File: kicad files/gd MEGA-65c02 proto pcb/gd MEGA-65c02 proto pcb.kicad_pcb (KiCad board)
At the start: 2 copper layers, 54 parts, among them J1 Pwr, J2 CTRL2, J3 Addr_Main_Data, J4 CTRL1, J5 Slot_Maker, J6 Aux Data_La, J7 CLKS, J8 14M_SEL, J9 PWR, Q1 Q_NPN_BCE-GET PACKAGE!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

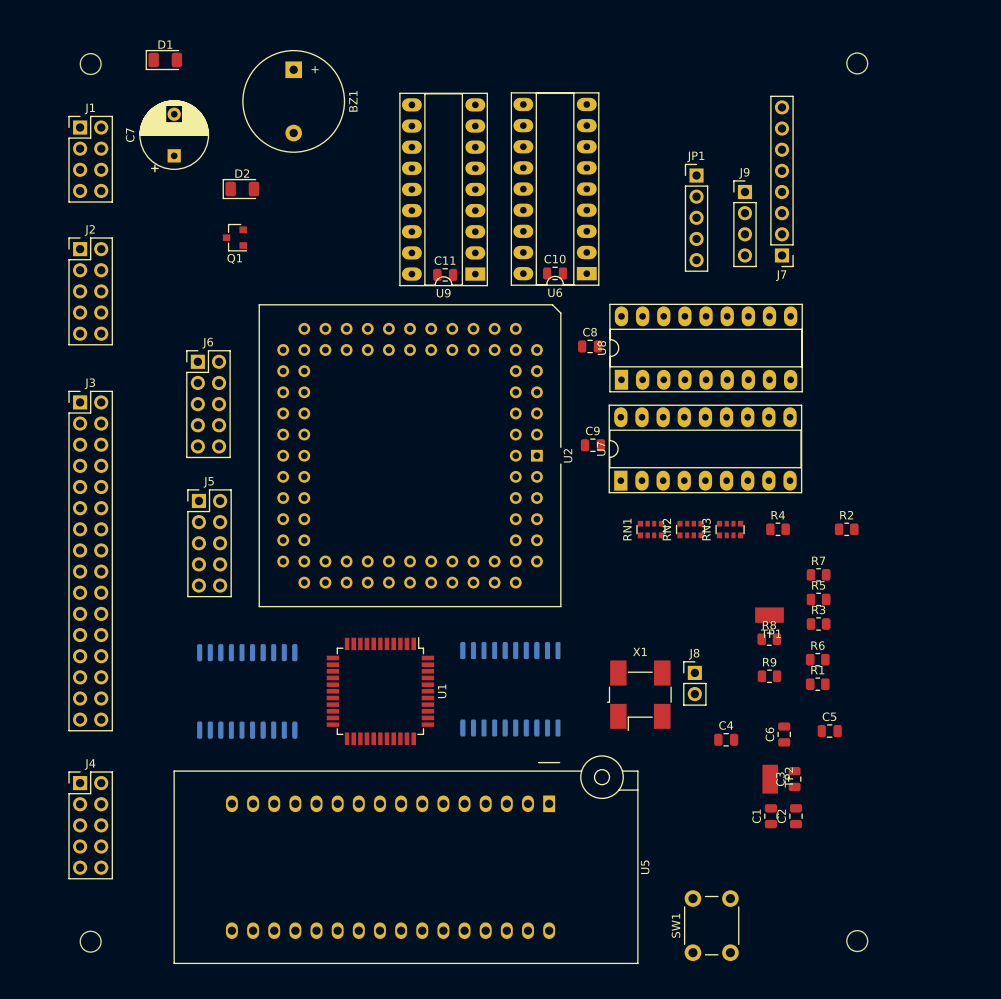
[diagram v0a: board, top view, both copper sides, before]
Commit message: started rev2 mega-6502 board design
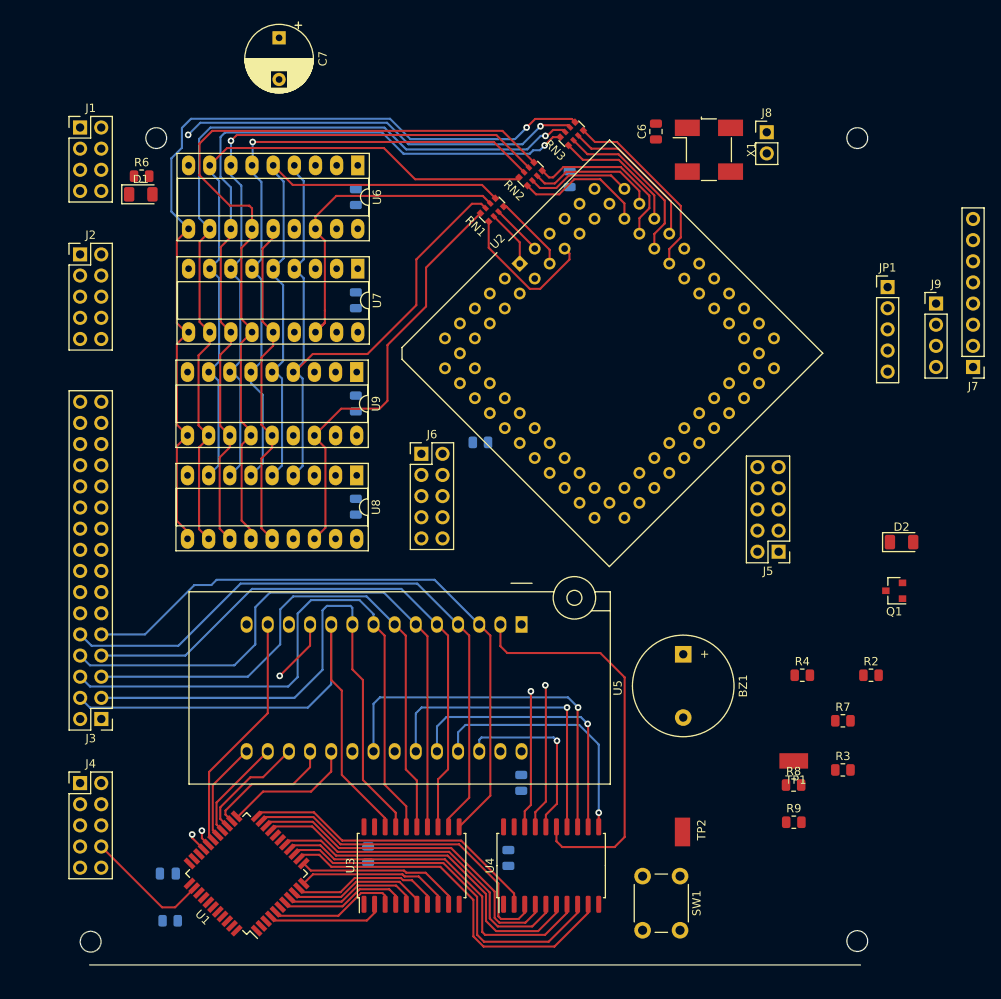
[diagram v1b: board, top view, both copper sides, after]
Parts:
- C1, C10, C11, C2, C3, C4, C5, C8, C9, R1, R5: moved to B.Cu
- U3, U4: moved to F.Cu
- U5: footprint Socket:DIP_Socket-32_W11.9_W12.7_W15.24_W17.78_W18.5_3M_232-1285-00-0602J -> Socket:DIP_Socket-28_W11.9_W12.7_W15.24_W17.78_W18.5_3M_228-1277-00-0602J
- moved R6 99.8 mm to (50.6, 52.2)
- moved D2 89.8 mm to (141.8, 96.2)
- moved Q1 89.8 mm to (141.0, 102.0)
- moved BZ1 84.4 mm to (115.6, 109.6)
- moved R1 82.8 mm to (54.0, 141.6)
- moved C6 74.0 mm to (112.3, 46.8)
- moved C5 73.3 mm to (102.0, 52.6), turned to 90 degrees
- moved J5 69.9 mm to (127.1, 97.3), turned to 180 degrees
- moved C4 69.0 mm to (53.7, 136.0), turned to 180 degrees
- moved X1 66.0 mm to (118.7, 49.0), turned to 270 degrees
- moved J8 65.5 mm to (125.7, 46.9)
- moved C2 51.6 mm to (77.8, 133.7), turned to 270 degrees
- moved RN3 51.2 mm to (102.2, 47.1), turned to 135 degrees
- moved RN2 46.8 mm to (97.3, 51.9), turned to 135 degrees
- moved R5 44.8 mm to (91.3, 84.2)
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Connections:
- RN1 pad 1: /CASM -> /CASA
- RN1 pad 2: /CASA -> /RAMWE
- RN1 pad 3: /RAS -> /CASM
- RN1 pad 4: /RAMWE -> /RAS
- RN1 pad 5: /RWE.B -> /RAS.B
- RN1 pad 6: /RAS.B -> /CASM.B
- RN1 pad 7: /CASA.B -> /RWE.B
- RN1 pad 8: /CASM.B -> /CASA.B
- RN2 pad 1: /RA0 -> /RA1
- RN2 pad 2: /RA3 -> /RA0
- RN2 pad 3: /RA6 -> /RA2
- RN2 pad 4: /RA7 -> /RA3
- RN2 pad 5: /RAF7 -> /RAF3
- RN2 pad 6: /RAF6 -> /RAF2
- RN2 pad 7: /RAF3 -> /RAF0
- RN2 pad 8: /RAF0 -> /RAF1
- RN3 pad 1: /RA1 -> /RA4
- RN3 pad 3: /RA2 -> /RA6
- RN3 pad 4: /RA4 -> /RA7
- RN3 pad 5: /RAF4 -> /RAF7
- RN3 pad 6: /RAF2 -> /RAF6
- RN3 pad 8: /RAF1 -> /RAF4
- U3 pad 11: /BA0 -> /BA7
- U3 pad 12: /BA1 -> /BA6
- U3 pad 13: /BA2 -> /BA5
- U3 pad 14: /BA3 -> /BA4
- U3 pad 15: /BA4 -> /BA3
- U3 pad 16: /BA5 -> /BA2
- U3 pad 17: /BA6 -> /BA1
- U3 pad 18: /BA7 -> /BA0
- U3 pad 2: /A7 -> /A0
- U3 pad 3: /A6 -> /A1
- U3 pad 4: /A5 -> /A2
- U3 pad 5: /A4 -> /A3
- U3 pad 6: /A3 -> /A4
- U3 pad 7: /A2 -> /A5
- U3 pad 8: /A1 -> /A6
- U3 pad 9: /A0 -> /A7
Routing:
- net /MD5: track 0.00 -> 187.7 mm
- net /MD1: track 0.00 -> 185.1 mm, vias 0 -> 1
- net /MD0: track 0.00 -> 179.6 mm, vias 0 -> 2
- net /MD7: track 0.00 -> 178.5 mm
- net /MD6: track 0.00 -> 168.8 mm
- net /MD2: track 0.00 -> 168.7 mm
- net /MD4: track 0.00 -> 168.5 mm
- net /MD3: track 0.00 -> 146.2 mm
- net /RAF6: track 0.00 -> 109.8 mm, vias 0 -> 2
- net /BA10: track 0.00 -> 107.2 mm, vias 0 -> 1
- net /BA12: track 0.00 -> 104.7 mm
- net /RAF7: track 0.00 -> 104.1 mm, vias 0 -> 1
- net /RAF5: track 0.00 -> 98.3 mm, vias 0 -> 1
- net /BA11: track 0.00 -> 98.3 mm, vias 0 -> 1
- net /RAF3: track 0.00 -> 96.9 mm
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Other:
- copper layers 2 -> 4

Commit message: added address bus to mega-2, routed clocks (minus vgc header), re-routed main data between ROM and backplane connectors, added several missing signals
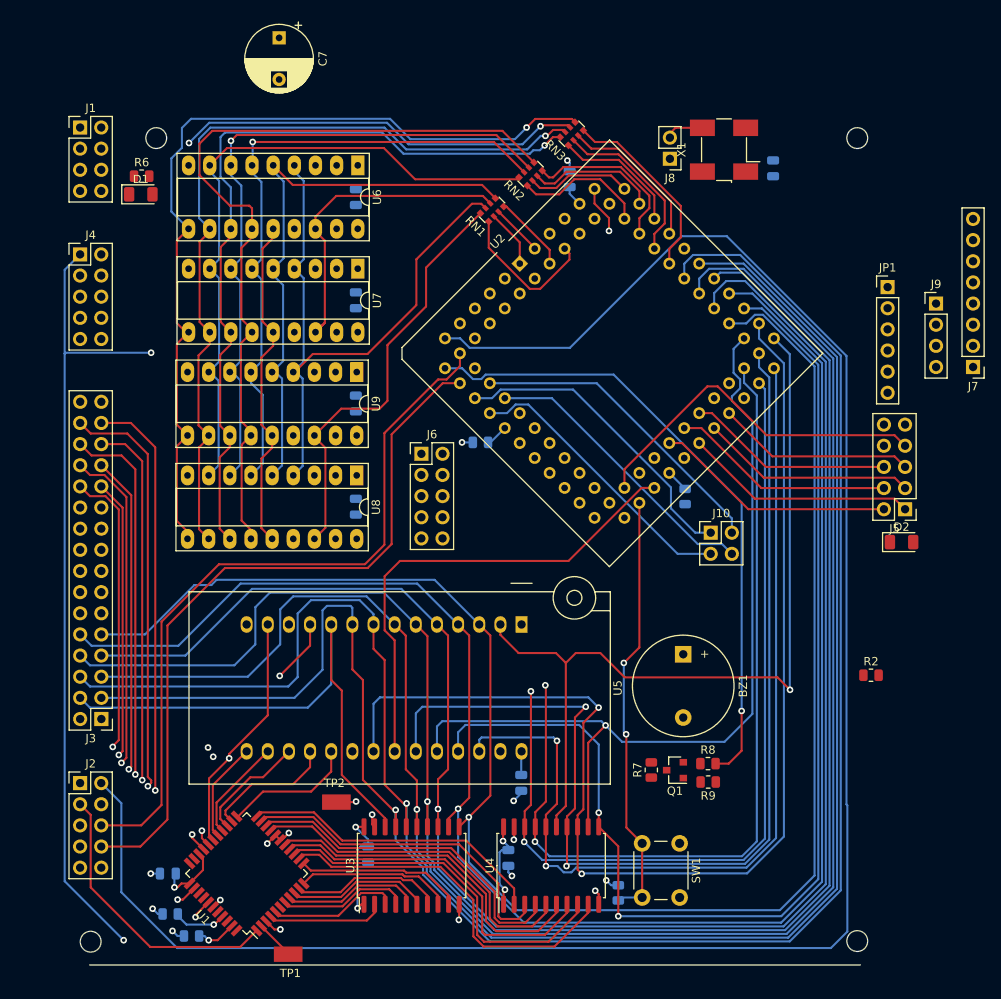
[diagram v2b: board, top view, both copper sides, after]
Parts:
- added J10: XY, Connector_PinHeader_2.54mm:PinHeader_2x02_P2.54mm_Vertical, F.Cu at (118.9, 95.0)
- added R10: 4k7, Resistor_SMD:R_0805_2012Metric, B.Cu at (115.8, 90.7)
- C6, R3, R4: moved to B.Cu
- JP1: footprint Connector_PinHeader_2.54mm:PinHeader_1x05_P2.54mm_Vertical -> Connector_PinHeader_2.54mm:PinHeader_1x06_P2.54mm_Vertical
- R5: value 3k3 -> 4k7
- moved R3 82.6 mm to (54.0, 140.8)
- moved TP1 65.0 mm to (68.2, 145.6)
- moved J2 63.5 mm to (43.2, 125.1)
- moved J4 63.5 mm to (43.2, 61.6)
- moved TP2 41.7 mm to (74.0, 127.4), turned to 180 degrees
- moved R4 34.2 mm to (107.8, 138.3), turned to 270 degrees
- moved Q1 34.0 mm to (114.6, 123.5)
- moved R7 23.8 mm to (111.8, 123.5), turned to 90 degrees
- moved J5 16.0 mm to (142.3, 92.2)
- moved C6 14.7 mm to (126.4, 51.3)
- moved J8 12.1 mm to (114.0, 50.1), turned to 180 degrees
- moved R9 11.4 mm to (118.6, 125.0), turned to 180 degrees
- moved R8 10.6 mm to (118.6, 122.8)
- moved SW1 3.94 mm to (115.2, 132.3)
- moved R1 3.15 mm to (56.6, 143.5)
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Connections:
- J2 pad 5: /!DMA -> /~DMA
- U2 pad 15: /IRQ -> /~IRQ
- U2 pad 37: /ROMEN -> /~ROMEN
- U2 pad 50: /SYNC -> /~SYNC
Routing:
- net /C060-67: track 0.00 -> 234.3 mm
- net /BA1: track 67.5 -> 222.9 mm, vias 0 -> 1
- net /~IRQ: track 0.00 -> 151.2 mm, vias 0 -> 3
- net /BA2: track 72.4 -> 221.7 mm, vias 0 -> 1
- net /PH0: track 15.1 -> 163.5 mm, vias 0 -> 1
- net /BA3: track 68.5 -> 216.8 mm, vias 0 -> 1
- net /BA4: track 73.5 -> 216.4 mm, vias 0 -> 1
- net /BA5: track 70.8 -> 212.1 mm, vias 0 -> 1
- net /BA6: track 77.0 -> 208.7 mm, vias 0 -> 1
- net /BA7: track 76.7 -> 202.2 mm, vias 0 -> 1
- net /~RESET: track 0.00 -> 112.8 mm, vias 0 -> 3
- net /BA8: track 92.4 -> 203.4 mm, vias 1 -> 2
- net /BA10: track 107.2 -> 205.5 mm, vias 1 -> 2
- net /BA11: track 98.3 -> 190.9 mm, vias 1 -> 2
- net /BA13: track 93.6 -> 184.5 mm, vias 1 -> 2
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
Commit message: Changed electrolytic to polymer-ta
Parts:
- added J11: 14M Enable, Connector_PinHeader_2.54mm:PinHeader_1x03_P2.54mm_Vertical, F.Cu at (127.1, 46.4)
- C7: footprint Capacitor_THT:CP_Radial_D8.0mm_P5.00mm -> Capacitor_Tantalum_SMD:CP_EIA-3216-18_Kemet-A_Pad1.58x1.35mm_HandSolder
- moved C6 8.23 mm to (118.8, 54.4), turned to 0 degrees
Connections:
- X1 pad 1: +5V -> Net-(J11-Pad2)
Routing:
- net Net-(J11-Pad2): track 0.00 -> 5.94 mm
- net +5V: track 45.9 -> 50.1 mm, vias 10 -> 11

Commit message: before trying to route clocks for video
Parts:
- BZ1: footprint Buzzer_Beeper:Buzzer_12x9.5RM7.6 -> My Libraries:12mm_Piezo_Buzzer
- C7: moved to B.Cu
- moved C7 23.5 mm to (50.5, 52.2), turned to 0 degrees
- moved BZ1 4.01 mm to (115.7, 113.6)
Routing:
- net +5V: track 50.1 -> 60.1 mm

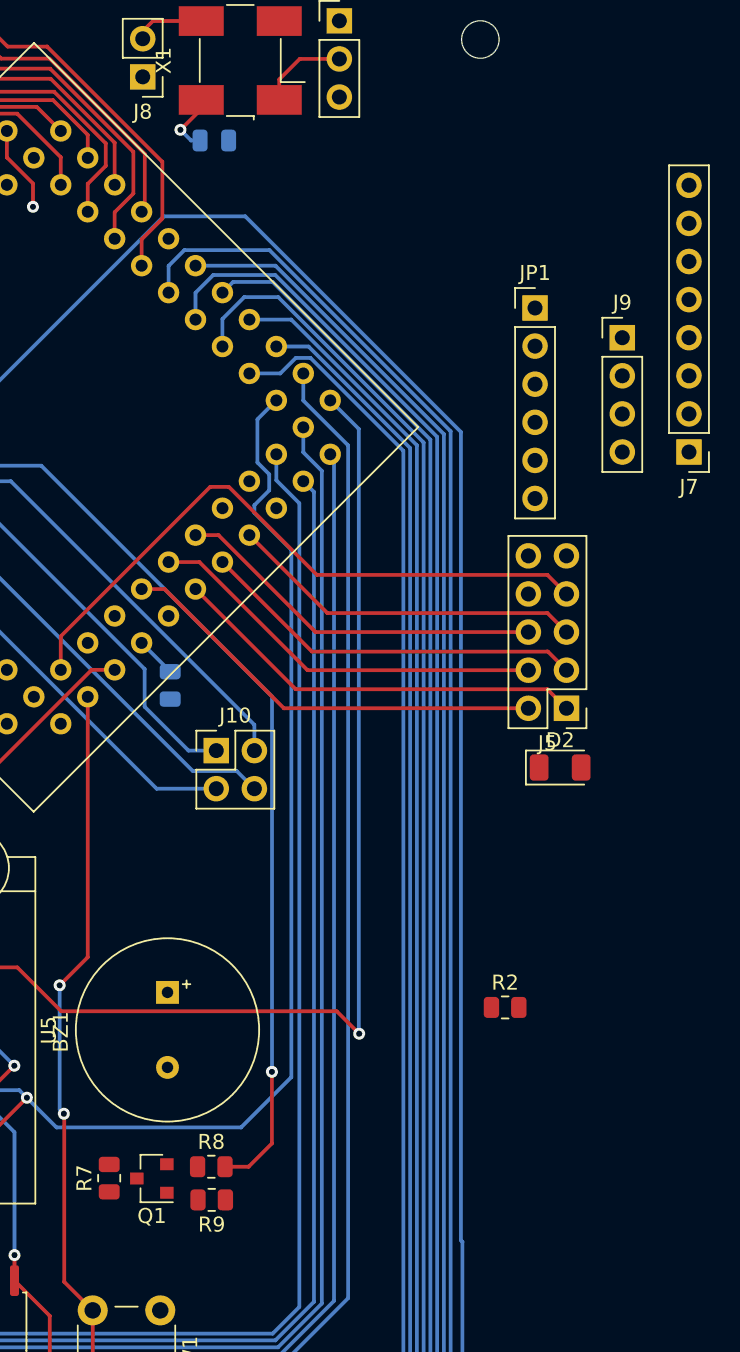
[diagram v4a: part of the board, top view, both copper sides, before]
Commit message: 111 to go: routed video clocks, changed video pin headers.
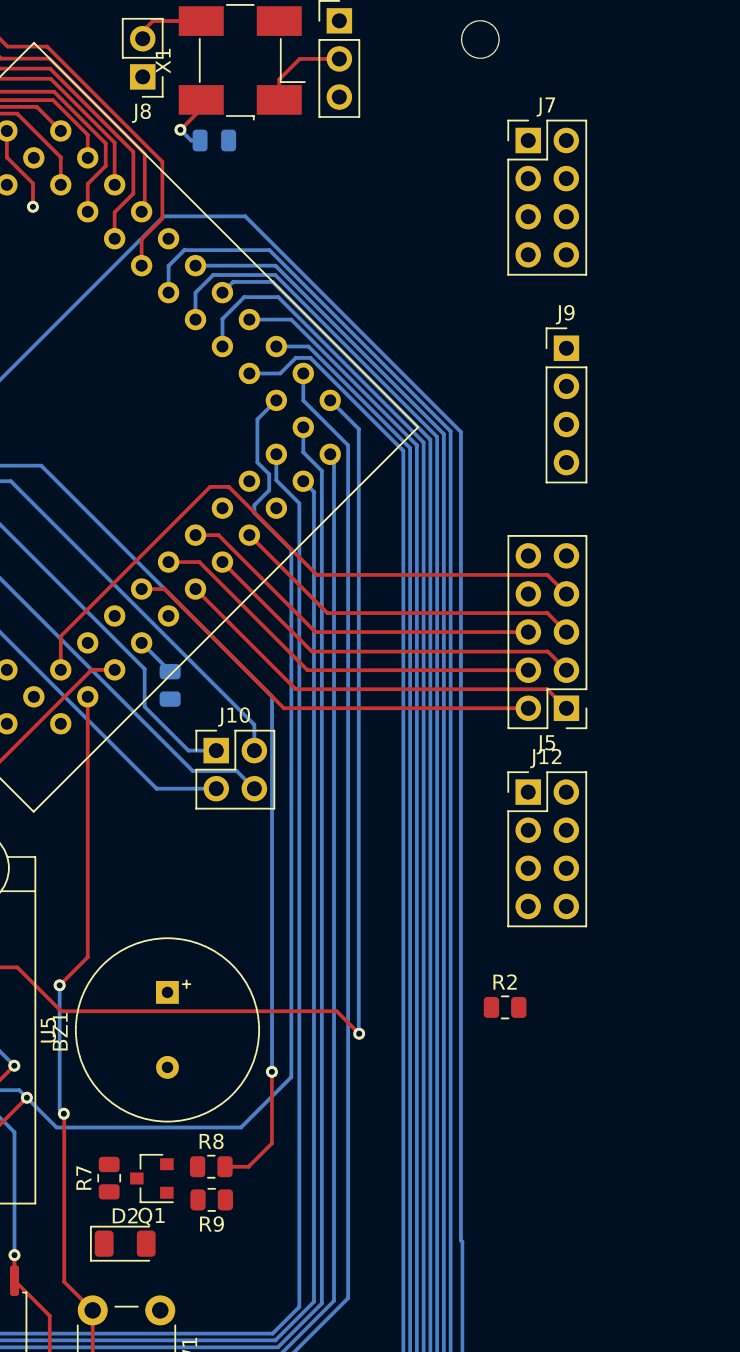
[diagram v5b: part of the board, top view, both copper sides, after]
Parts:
- removed JP1: RGB Binary, Connector_PinHeader_2.54mm:PinHeader_1x06_P2.54mm_Vertical
- added J12: RGB Bin, Connector_PinHeader_2.54mm:PinHeader_2x04_P2.54mm_Vertical, F.Cu at (139.7, 97.8)
- J7: footprint Connector_PinHeader_2.54mm:PinHeader_1x08_P2.54mm_Vertical -> Connector_PinHeader_2.54mm:PinHeader_2x04_P2.54mm_Vertical
- moved D2 43.0 mm to (112.9, 127.9)
- moved J7 23.4 mm to (139.7, 54.4), turned to 0 degrees
- moved J9 3.79 mm to (142.3, 68.2)
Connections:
- J7 pad 2: GND -> /7M
- J7 pad 3: /7M -> /CREF
- J7 pad 4: /CREF -> /Q3
- J7 pad 5: /Q3 -> /PH0
- J7 pad 6: /PH0 -> /~RESET
- J7 pad 7: /~RESET -> GND
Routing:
- net /PH0: track 163.5 -> 206.4 mm
- net /Q3: track 81.0 -> 122.7 mm
- net /CREF: track 77.0 -> 118.1 mm
- net /7M: track 79.0 -> 118.2 mm
- net /14M: track 13.6 -> 43.7 mm

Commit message: 106 to go: got X below 100mm!
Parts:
- R4: moved to F.Cu
- moved H4 6.65 mm to (142.7, 141.7)
- moved H2 6.23 mm to (142.7, 47.4)
- moved TP1 4.59 mm to (72.0, 143.1)
- moved R1 4.33 mm to (52.5, 142.1), turned to 180 degrees
- moved H1 3.32 mm to (42.2, 141.7)
- moved R3 1.93 mm to (52.3, 139.8)
- turned R4 to 90 degrees
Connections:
- J12 pad 1: /RGB4 -> /~SYNC
- J12 pad 2: /RGB2 -> /RGB4
- J12 pad 3: /RGB8 -> /RGB1
- J12 pad 4: /~SYNC -> /RGB8
- J12 pad 5: /RGB1 -> /RGB2
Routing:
- net /RW: track 0.00 -> 241.3 mm, vias 0 -> 3
- net /RGB1: track 0.00 -> 58.8 mm
- net /~SYNC: track 0.00 -> 48.5 mm
- net /RGB4: track 0.00 -> 44.3 mm
- net /RGB8: track 0.00 -> 43.8 mm
- net /RGB2: track 0.00 -> 38.7 mm
- net GND: track 19.8 -> 4.63 mm, vias 10 -> 2
- net +5V: track 60.1 -> 46.0 mm, vias 11 -> 6
- net /BA8: track 203.4 -> 195.5 mm
- net /~RESET: track 112.8 -> 108.3 mm
- net /BA7: track 202.2 -> 198.1 mm
- net /BA6: track 208.7 -> 204.8 mm
- net /C060-67: track 234.3 -> 231.2 mm
- net /65_SYNC: track 4.73 -> 7.42 mm
- net /BA5: track 212.1 -> 209.8 mm
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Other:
- board outline added: 106.2 x 99.9 mm
- board text added: "MD2"
- board text added: "Q3"
